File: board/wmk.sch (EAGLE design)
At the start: 22 parts, among them IC1 LM1117MPX-3.3, U2 STM32F103C8T6, X1 PN87520-S

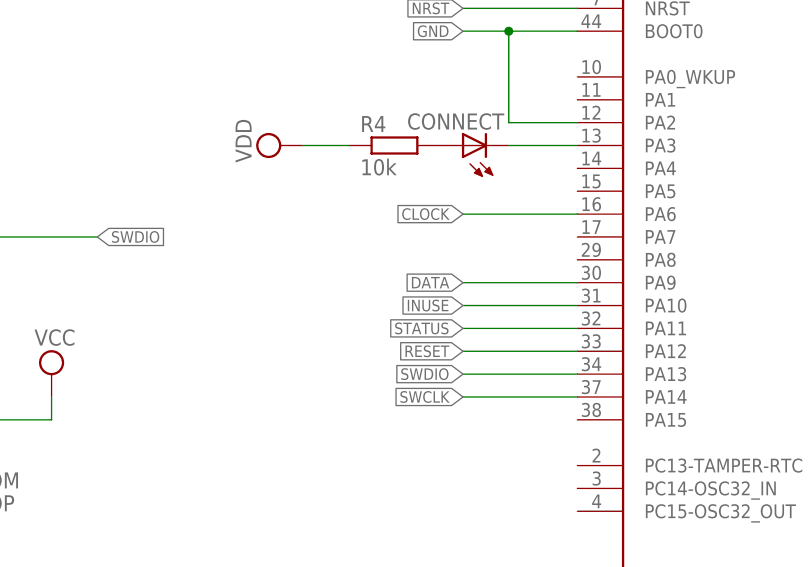
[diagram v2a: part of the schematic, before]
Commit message: Added TX/RX and moved LEDS
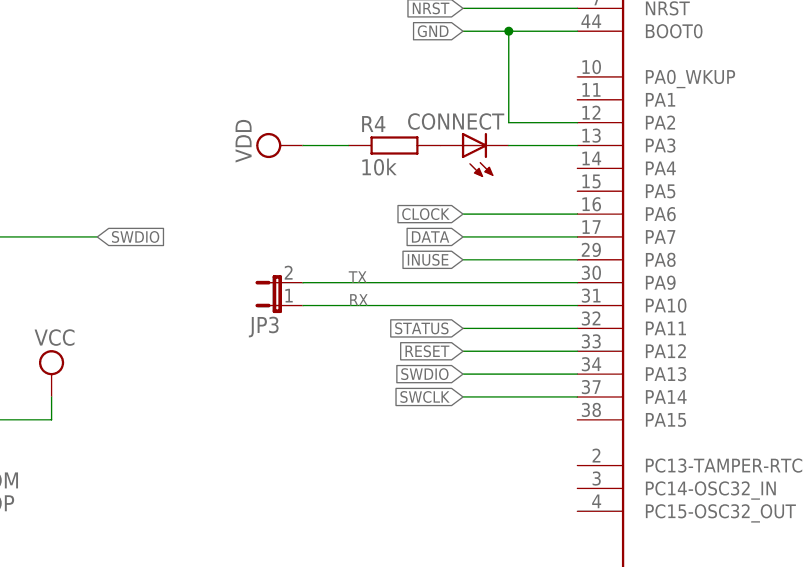
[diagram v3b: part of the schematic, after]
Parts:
- added JP3: (no value), jumper:JP1E
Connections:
- new net RX: JP3.1, U2.PA10
- new net TX: JP3.2, U2.PA9
- net DATA: now also U2.PA7; no longer U2.PA9
- net INUSE: now also U2.PA8; no longer U2.PA10
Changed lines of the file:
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@@
 <part name="U2" library="STM32F103C8T6" deviceset="STM32F103C8T6" device=""/>
 <part name="F1" library="eagle-ltspice" library_urn="urn:adsk.eagle:library:217" deviceset="R" device="R1206" package3d_urn="urn:adsk.eagle:package:13301/1"/>
+<part name="JP3" library="jumper" library_urn="urn:adsk.eagle:library:252" deviceset="JP1E" device="" package3d_urn="urn:adsk.eagle:package:15455/1"/>
 </parts>
 <sheets>
@@
 <attribute name="NAME" x="-135.89" y="39.1414" size="1.778" layer="95" rot="R180"/>
 <attribute name="VALUE" x="-135.89" y="43.942" size="1.778" layer="96" rot="R180"/>
+</instance>
+<instance part="JP3" gate="A" x="-99.06" y="53.34" smashed="yes" rot="R90">
+<attribute name="NAME" x="-99.06" y="52.07" size="1.778" layer="95" rot="R180"/>
+<attribute name="VALUE" x="-99.06" y="59.055" size="1.778" layer="96" rot="R180"/>
 </instance>
 </instances>
@@
 </segment>
 <segment>
-<label x="-78.74" y="55.88" size="1.27" layer="95" rot="R180" xref="yes"/>
-<pinref part="U2" gate="G$1" pin="PA9"/>
-<wire x1="-66.04" y1="55.88" x2="-78.74" y2="55.88" width="0.1524" layer="91"/>
+<pinref part="U2" gate="G$1" pin="PA7"/>
+<wire x1="-66.04" y1="60.96" x2="-78.74" y2="60.96" width="0.1524" layer="91"/>
+<label x="-78.74" y="60.96" size="1.27" layer="95" rot="R180" xref="yes"/>
 </segment>
 </net>
@@
 </segment>
 <segment>
-<label x="-78.74" y="53.34" size="1.27" layer="95" rot="R180" xref="yes"/>
-<pinref part="U2" gate="G$1" pin="PA10"/>
-<wire x1="-66.04" y1="53.34" x2="-78.74" y2="53.34" width="0.1524" layer="91"/>
+<wire x1="-66.04" y1="58.42" x2="-78.74" y2="58.42" width="0.1524" layer="91"/>
+<pinref part="U2" gate="G$1" pin="PA8"/>
+<label x="-78.74" y="58.42" size="1.27" layer="95" rot="R180" xref="yes"/>
 </segment>
 </net>
@@
 </segment>
 </net>
+<net name="TX" class="0">
+<segment>
+<pinref part="JP3" gate="A" pin="2"/>
+<pinref part="U2" gate="G$1" pin="PA9"/>
+<wire x1="-96.52" y1="55.88" x2="-66.04" y2="55.88" width="0.1524" layer="91"/>
+<label x="-91.44" y="55.88" size="1.27" layer="95"/>
+</segment>
+</net>
+<net name="RX" class="0">
+<segment>
+<pinref part="JP3" gate="A" pin="1"/>
+<pinref part="U2" gate="G$1" pin="PA10"/>
+<wire x1="-96.52" y1="53.34" x2="-66.04" y2="53.34" width="0.1524" layer="91"/>
+<label x="-91.44" y="53.34" size="1.27" layer="95"/>
+</segment>
+</net>
